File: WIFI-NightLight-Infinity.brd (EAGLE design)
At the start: 49.2 x 44.4 mm, 56 parts, among them CN1 PBS-3-VERTICAL, CN2 PBS-2-VERTICAL, CN5 PBS-2-VERTICAL, CN6 PBS-2-VERTICAL, CN7 PBS-4-VERTICAL, IC3 MC34063AD, IC4 DS1307Z, M1 ESP8266-12F, Q1 32.768K, T2 BC847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

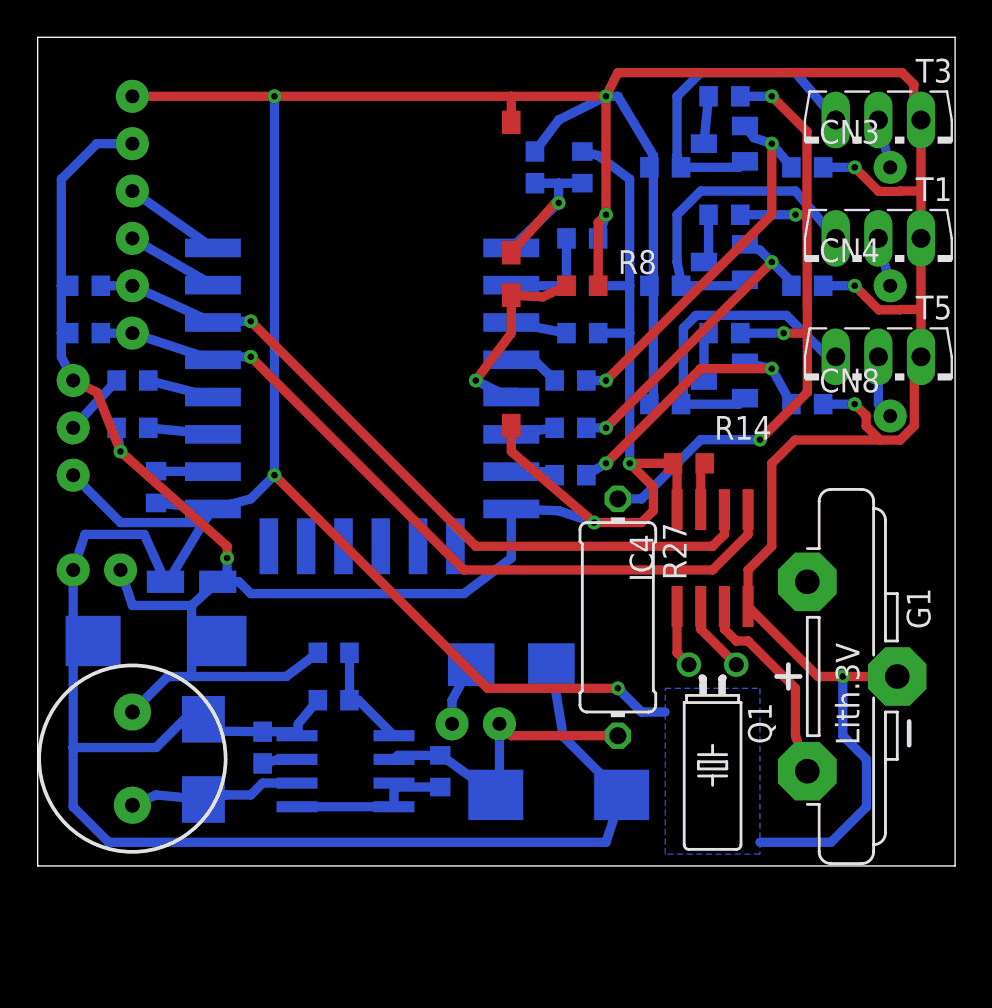
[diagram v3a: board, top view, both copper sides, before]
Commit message: Errors were fixed
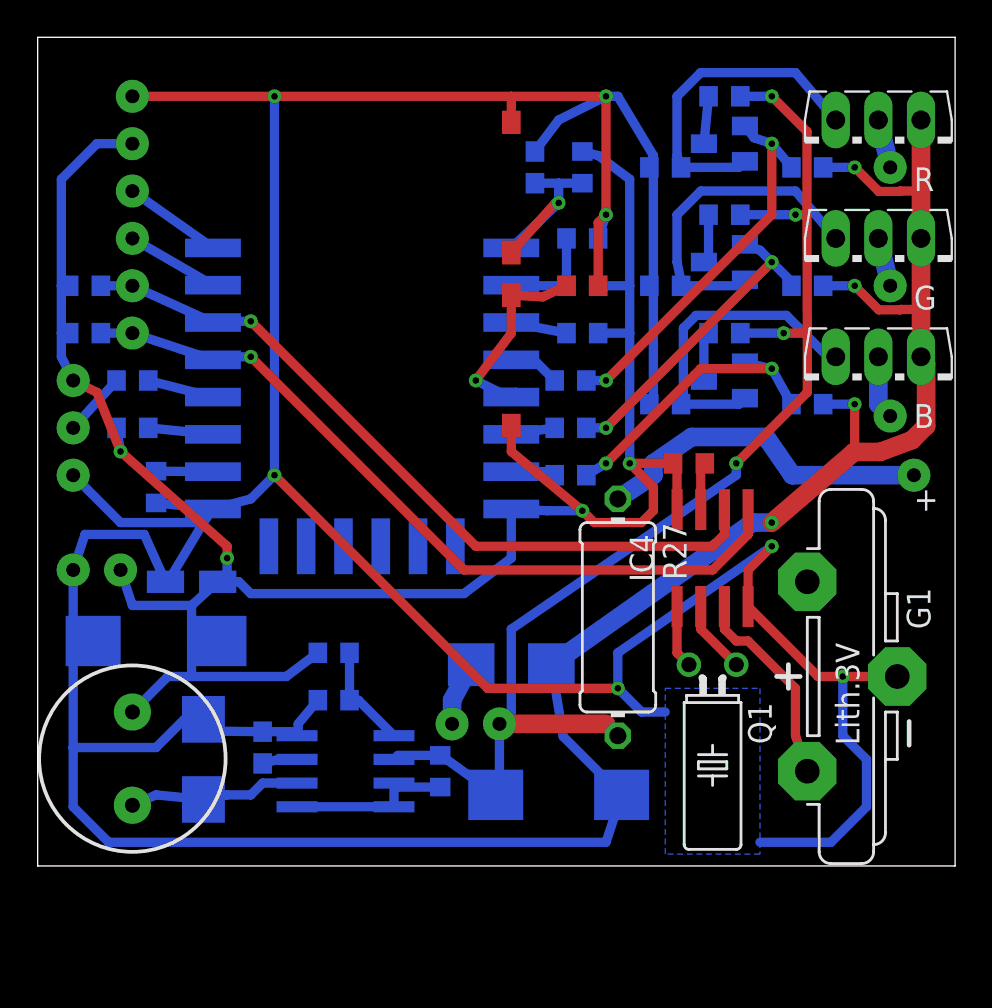
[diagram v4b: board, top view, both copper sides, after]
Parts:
- added CN9: +, pls:PBS-1-VERTICAL
- CN3: value (none) -> R
- CN4: value (none) -> G
- CN8: value (none) -> B
- R15, R19, R23: value 100K -> 1K
- R16, R17, R18, R20, R21, R22, R24, R25, R26: value 100K -> 10K
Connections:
- removed net N$21: R17.2, R22.2, R26.2, R27.1
- new net N$20: CN9.P$1, R27.1
- net +5V: now also R17.2, R22.2, R26.2
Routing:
- net +5V: track 17.0 -> 68.5 mm, vias 0 -> 4
- net N$21: track 38.0 -> 0.00 mm, vias 4 -> 0
- net N$20: track 0.00 -> 18.4 mm
- net GND: track 299.9 -> 303.7 mm, vias 9 -> 11
- net +3V3: track 121.3 -> 120.6 mm

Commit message: Preparing for production.
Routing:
- net GND: track 303.7 -> 287.0 mm, vias 11 -> 10
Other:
- board text added: "Polyakov Konstantin Russia, Yeysk, 2018-09-16, WFNLI-1-1"
- board text removed: "Polyakov Konstantin Russia, Yeysk, 2018-09-16, v0.1 rev1"
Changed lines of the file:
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@@
 <?xml version="1.0" encoding="utf-8"?>
 <!DOCTYPE eagle SYSTEM "eagle.dtd">
-<eagle version="8.5.2">
+<eagle version="9.1.3">
 <drawing>
 <settings>
@@
 <text x="5.08" y="24.13" size="1.2" layer="27" font="vector" ratio="12">| Boot</text>
 <text x="22.225" y="23.495" size="1.2" layer="27" font="vector" ratio="12" rot="R90">RST sets</text>
-<text x="9.525" y="40.64" size="1.2" layer="27" font="vector" ratio="12">Polyakov Konstantin
-Russia, Yeysk, 2018-09-16, v0.1 rev1</text>
+<text x="7.62" y="40.64" size="1.2" layer="27" font="vector" ratio="12">Polyakov Konstantin
+Russia, Yeysk, 2018-09-16, WFNLI-1-1</text>
 <text x="22.225" y="33.655" size="1.27" layer="27" font="vector" ratio="12" rot="R90">Reboot</text>
 <text x="0.635" y="30.48" size="1.2" layer="27" font="vector" ratio="12" rot="SR0">SCL</text>
@@
 <param name="checkStop" value="0"/>
 <param name="checkValues" value="0"/>
+<param name="checkNames" value="1"/>
+<param name="checkWireStubs" value="1"/>
+<param name="checkPolygonWidth" value="0"/>
 <param name="useDiameter" value="13"/>
 <param name="maxErrors" value="50"/>
@@
 <attribute name="SPICEMODEL" value="NONE" x="28.575" y="26.035" size="1.2" layer="28" rot="MR0" display="off"/>
 <attribute name="SPICEPREFIX" value="R" x="28.575" y="26.035" size="1.2" layer="28" rot="MR0" display="off"/>
-<attribute name="VALUE" x="29.845" y="24.13" size="1.27" layer="28" rot="MR0"/>
+<attribute name="VALUE" x="23.495" y="24.13" size="1.27" layer="28" font="vector" ratio="12" rot="MR0"/>
 </element>
 <element name="R18" library="eagle-ltspice" library_urn="urn:adsk.eagle:library:217" package="R0603" package3d_urn="urn:adsk.eagle:package:13302/1" value="10K" x="41.275" y="37.465" smashed="yes" rot="MR0">
@@
 </element>
 <element name="CN3" library="pls" package="PBS-1-VERTICAL" value="R" x="45.72" y="37.465" smashed="yes">
-<attribute name="VALUE" x="46.99" y="36.195" size="1.27" layer="21"/>
+<attribute name="VALUE" x="46.99" y="36.195" size="1.27" layer="21" font="vector" ratio="12"/>
 </element>
 <element name="T1" library="transistor" library_urn="urn:adsk.eagle:library:402" package="TO126V" package3d_urn="urn:adsk.eagle:package:29912/1" value="" x="45.085" y="32.385" smashed="yes" rot="R180">
@@
 <attribute name="SPICEMODEL" value="NONE" x="48.26" y="26.035" size="1.2" layer="28" rot="MR0" display="off"/>
 <attribute name="SPICEPREFIX" value="R" x="48.26" y="26.035" size="1.2" layer="28" rot="MR0" display="off"/>
-<attribute name="VALUE" x="29.845" y="21.59" size="1.27" layer="28" rot="MR0"/>
+<attribute name="VALUE" x="23.495" y="21.59" size="1.27" layer="28" font="vector" ratio="12" rot="MR0"/>
 </element>
 <element name="R20" library="eagle-ltspice" library_urn="urn:adsk.eagle:library:217" package="R0603" package3d_urn="urn:adsk.eagle:package:13302/1" value="10K" x="41.275" y="31.115" smashed="yes" rot="MR0">
@@
 </element>
 <element name="CN4" library="pls" package="PBS-1-VERTICAL" value="G" x="45.72" y="31.115" smashed="yes">
-<attribute name="VALUE" x="46.99" y="29.845" size="1.27" layer="21"/>
+<attribute name="VALUE" x="46.99" y="29.845" size="1.27" layer="21" font="vector" ratio="12"/>
 </element>
 <element name="T5" library="transistor" library_urn="urn:adsk.eagle:library:402" package="TO126V" package3d_urn="urn:adsk.eagle:package:29912/1" value="" x="45.085" y="26.035" smashed="yes" rot="R180">
@@
 <attribute name="SPICEMODEL" value="NONE" x="28.575" y="31.115" size="1.2" layer="28" rot="MR0" display="off"/>
 <attribute name="SPICEPREFIX" value="R" x="28.575" y="31.115" size="1.2" layer="28" rot="MR0" display="off"/>
-<attribute name="VALUE" x="29.845" y="19.05" size="1.27" layer="28" rot="MR0"/>
+<attribute name="VALUE" x="23.495" y="19.05" size="1.27" layer="28" font="vector" ratio="12" rot="MR0"/>
 </element>
 <element name="R24" library="eagle-ltspice" library_urn="urn:adsk.eagle:library:217" package="R0603" package3d_urn="urn:adsk.eagle:package:13302/1" value="10K" x="41.275" y="24.765" smashed="yes" rot="MR0">
@@
 </element>
 <element name="CN8" library="pls" package="PBS-1-VERTICAL" value="B" x="45.72" y="24.13" smashed="yes">
-<attribute name="VALUE" x="46.99" y="23.495" size="1.27" layer="21"/>
+<attribute name="VALUE" x="46.99" y="23.495" size="1.27" layer="21" font="vector" ratio="12"/>
 </element>
 <element name="R27" library="resistor" library_urn="urn:adsk.eagle:library:348" package="0411/12" package3d_urn="urn:adsk.eagle:package:26091/1" value="" x="31.115" y="13.335" rot="R270"/>
 <element name="CN9" library="pls" package="PBS-1-VERTICAL" value="+" x="46.99" y="20.955" smashed="yes">
-<attribute name="VALUE" x="46.99" y="19.05" size="1.27" layer="21"/>
+<attribute name="VALUE" x="46.99" y="19.05" size="1.27" layer="21" font="vector" ratio="12"/>
 </element>
 </elements>
@@
 <contactref element="D2" pad="A"/>
 <wire x1="1.905" y1="11.43" x2="2.975" y2="12.065" width="0.5" layer="16"/>
-<wire x1="28.185" y1="6.94" x2="27.55" y2="10.795" width="0.5" layer="16"/>
-<wire x1="31.315" y1="3.81" x2="28.185" y2="6.94" width="0.5" layer="16"/>
+<wire x1="27.55" y1="10.795" x2="28.185" y2="6.94" width="0.5" layer="16"/>
 <contactref element="BTN2" pad="1"/>
 <wire x1="25.4" y1="39.878" x2="25.4" y2="41.275" width="0.5" layer="1"/>
 <contactref element="IC4" pad="4"/>
 <contactref element="G1" pad="-"/>
-<wire x1="39.37" y1="17.145" x2="38.1" y2="15.875" width="0.5" layer="1"/>
-<wire x1="38.1" y1="15.875" x2="38.1" y2="13.91" width="0.5" layer="1"/>
 <wire x1="5.08" y1="41.275" x2="12.7" y2="41.275" width="0.5" layer="1"/>
 <wire x1="38.1" y1="13.91" x2="41.85" y2="10.16" width="0.5" layer="1"/>
 <wire x1="41.85" y1="10.16" x2="43.18" y2="10.16" width="0.5" layer="1"/>
 <wire x1="43.18" y1="10.16" x2="46.101" y2="10.16" width="0.5" layer="1"/>
-<wire x1="31.315" y1="3.81" x2="31.95" y2="4.445" width="0.5" layer="16"/>
 <polygon width="0.2" layer="16">
 <vertex x="33.655" y="9.525"/>
@@
 <wire x1="47.371" y1="40.005" x2="47.371" y2="36.195" width="1" layer="1"/>
 <wire x1="47.371" y1="36.195" x2="47.371" y2="33.655" width="1" layer="1"/>
-<wire x1="43.89368125" y1="31.115" x2="43.815" y2="31.115" width="0.5" layer="1"/>
 <wire x1="46.25491875" y1="36.1736" x2="46.27631875" y2="36.195" width="0.5" layer="1"/>
 <wire x1="46.27631875" y1="36.195" x2="47.371" y2="36.195" width="0.5" layer="1"/>
@@
 <wire x1="46.25491875" y1="29.8236" x2="46.27631875" y2="29.845" width="0.5" layer="1"/>
 <wire x1="46.27631875" y1="29.845" x2="47.371" y2="29.845" width="0.5" layer="1"/>
-<wire x1="43.815" y1="31.115" x2="45.1064" y2="29.8236" width="0.5" layer="1"/>
-<wire x1="45.1064" y1="29.8236" x2="46.25491875" y2="29.8236" width="0.5" layer="1"/>
+<wire x1="46.25491875" y1="29.8236" x2="45.1064" y2="29.8236" width="0.5" layer="1"/>
 <wire x1="42.125" y1="24.765" x2="43.815" y2="24.765" width="0.5" layer="16"/>
 <via x="43.815" y="24.765" extent="1-16" drill="0.35"/>
@@
 <wire x1="43.815" y1="22.2036" x2="45.18508125" y2="22.2036" width="1" layer="1"/>
 <wire x1="43.815" y1="24.765" x2="43.815" y2="22.2036" width="0.5" layer="1"/>
-<via x="39.37" y="17.145" extent="1-16" drill="0.35"/>
-<wire x1="31.115" y1="9.525" x2="31.115" y2="11.43" width="0.5" layer="16"/>
-<wire x1="31.115" y1="11.43" x2="39.37" y2="17.145" width="0.5" layer="16"/>
 <via x="39.37" y="18.415" extent="1-16" drill="0.35"/>
 <wire x1="27.55" y1="10.795" x2="38.345" y2="18.415" width="1" layer="16"/>
 <wire x1="38.345" y1="18.415" x2="39.37" y2="18.415" width="1" layer="16"/>
+<wire x1="45.1064" y1="29.8236" x2="43.815" y2="31.115" width="0.5" layer="1"/>
+<wire x1="28.185" y1="6.94" x2="31.315" y2="3.81" width="0.5" layer="16"/>
 </signal>
 <signal name="+3V3">
@@
 <contactref element="R9" pad="1"/>
 <contactref element="IC3" pad="5"/>
-<wire x1="19.265" y1="6.985" x2="19.11" y2="6.985" width="0.5" layer="16"/>
-<wire x1="19.05" y1="6.985" x2="19.11" y2="6.985" width="0.5" layer="16"/>
 <wire x1="19.11" y1="6.985" x2="17.205" y2="8.89" width="0.5" layer="16"/>
 <wire x1="17.205" y1="8.89" x2="16.725" y2="8.89" width="0.5" layer="16"/>
@@
 </signal>
 </signals>
+<mfgpreviewcolors>
+<mfgpreviewcolor name="soldermaskcolor" color="0xC8008000"/>
+<mfgpreviewcolor name="silkscreencolor" color="0xFFFEFEFE"/>
+<mfgpreviewcolor name="backgroundcolor" color="0xFF282828"/>
+<mfgpreviewcolor name="coppercolor" color="0xFFFFBF00"/>
+<mfgpreviewcolor name="substratecolor" color="0xFF786E46"/>
+</mfgpreviewcolors>
 </board>
 </drawing>

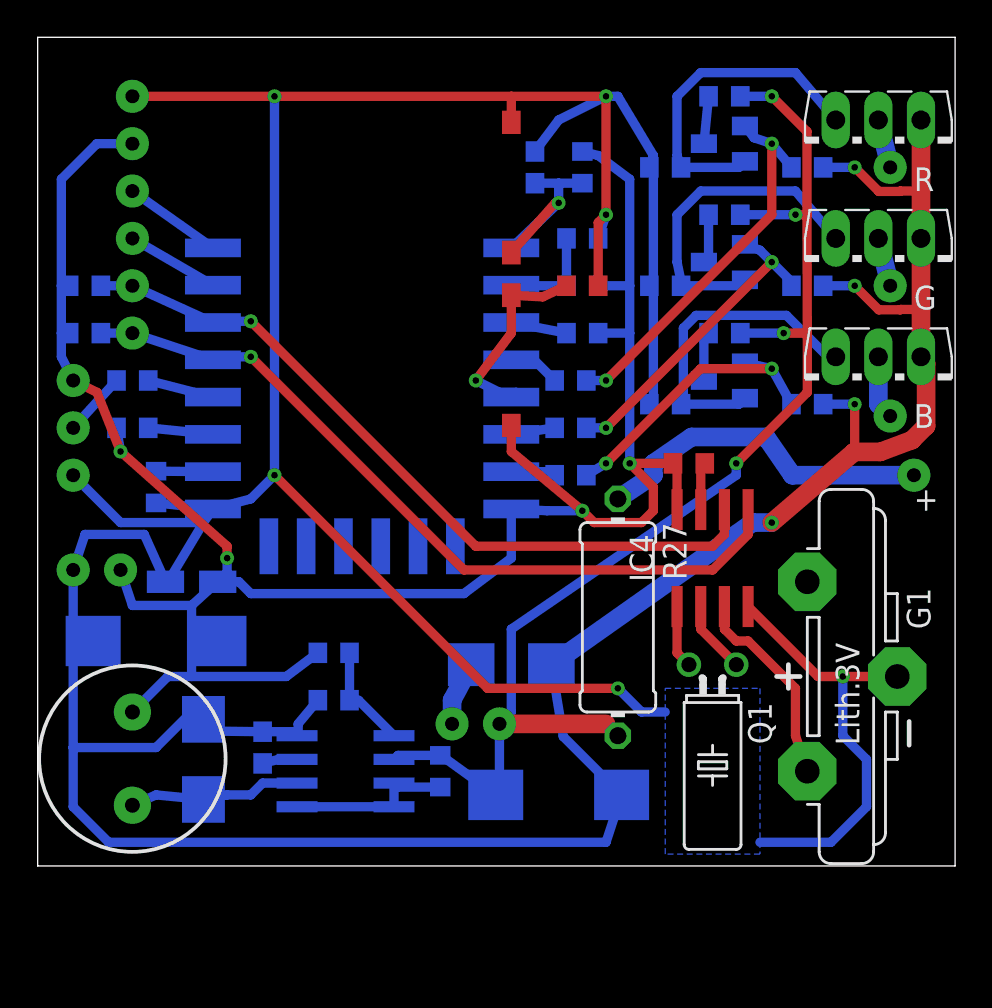
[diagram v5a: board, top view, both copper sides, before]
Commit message: Value was changed. Updating for Eagle 9.2.0
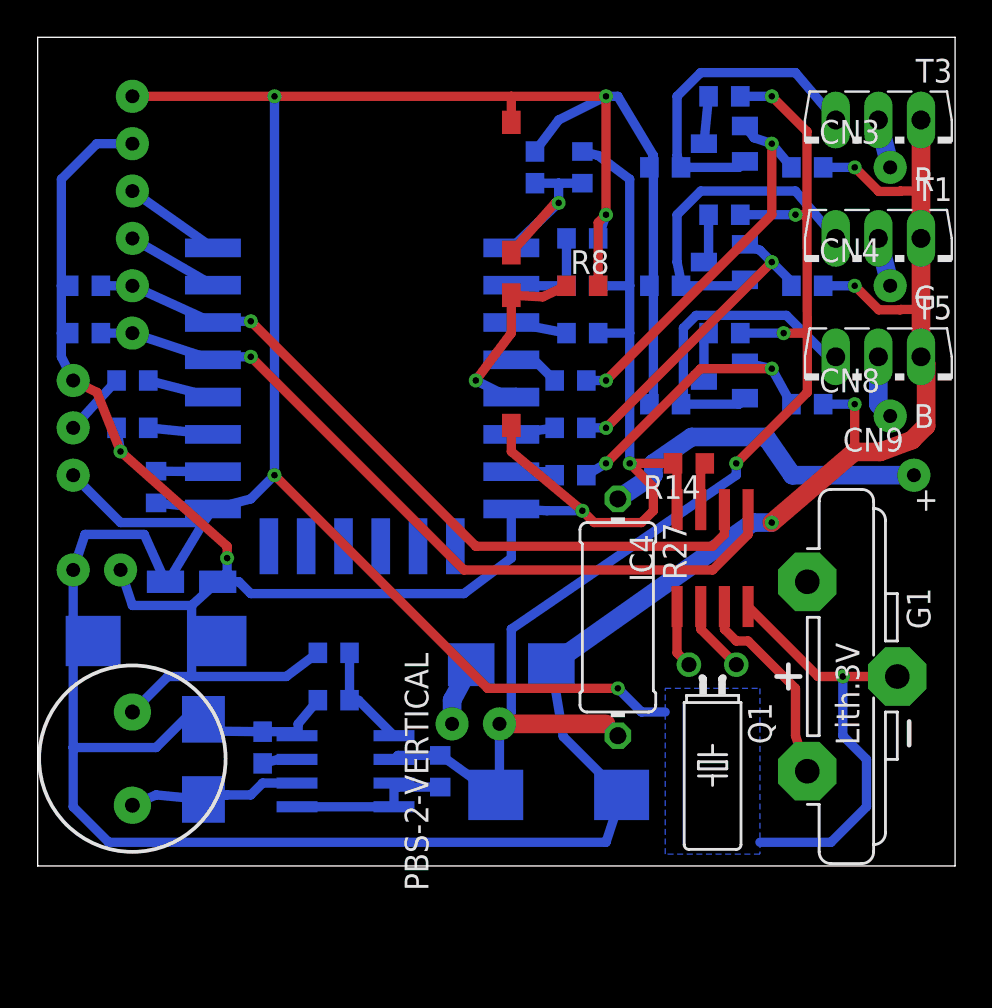
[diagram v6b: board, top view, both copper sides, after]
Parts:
- R10: value 5.1k -> 5.6k
- R27: value (none) -> 56
